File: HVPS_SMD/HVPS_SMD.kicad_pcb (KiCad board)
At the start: 2 copper layers, 30 x 20 mm, 18 parts, among them J1 CONN_01X02, J2 CONN_01X02, Q1 AO4294, T1 MagTop-HVSMPS, U1 LM3478SOIC8

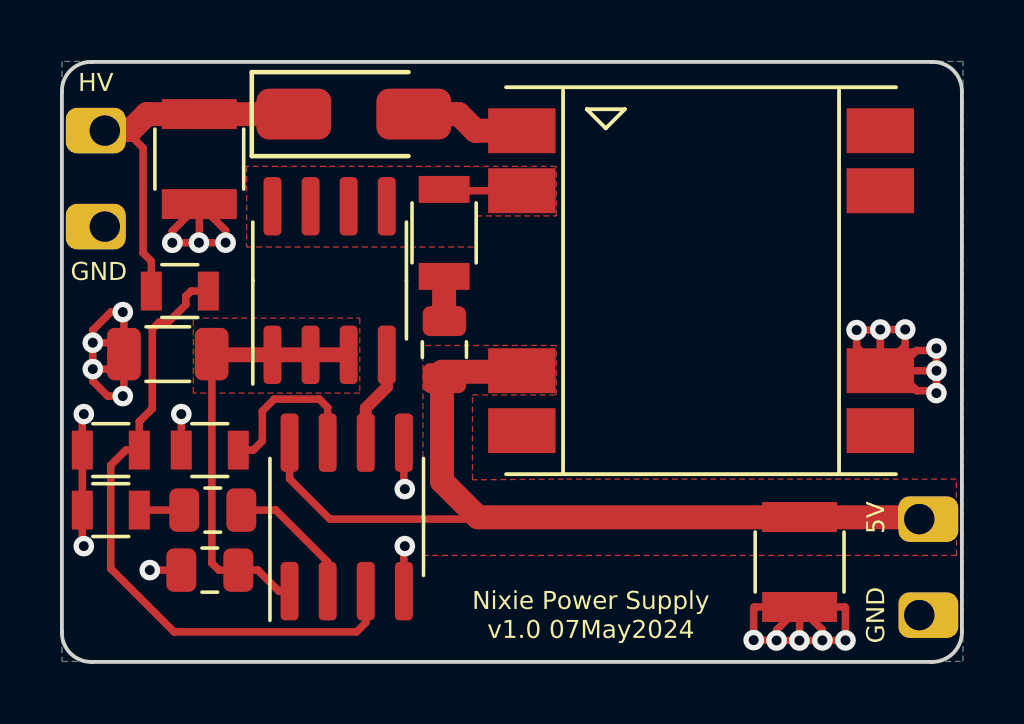
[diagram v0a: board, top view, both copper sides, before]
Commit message: Add fiducials and external control options
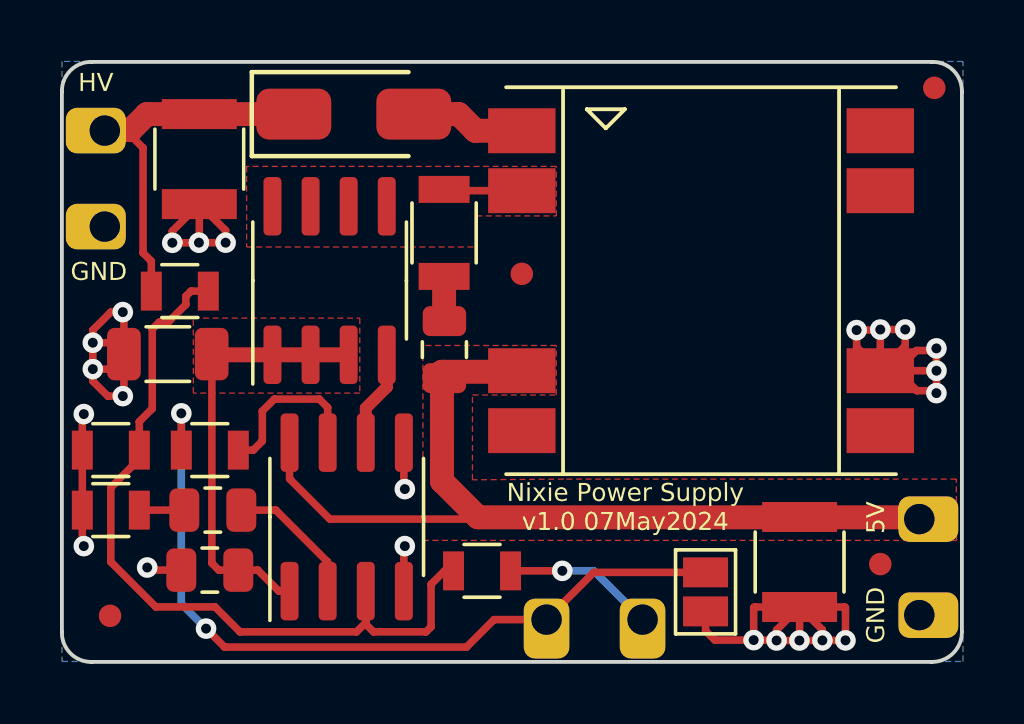
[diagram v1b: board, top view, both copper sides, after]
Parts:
- removed G***: LOGO-Nixieclock.biz, NixieClockMaster:LOGO-Nixieclock.biz
- added FID1: Fiducial, Fiducial:Fiducial_0.75mm_Mask1.5mm, F.Cu at (212.3, 77.9)
- added FID2: Fiducial, Fiducial:Fiducial_0.75mm_Mask1.5mm, F.Cu at (214.2, 62.0)
- added FID3: Fiducial, Fiducial:Fiducial_0.75mm_Mask1.5mm, F.Cu at (200.4, 68.2)
- added FID4: Fiducial, Fiducial:Fiducial_0.75mm_Mask1.5mm, F.Cu at (186.7, 79.6)
- added J3: CONN_01X02, NixieClockMaster:Header_MA02-Edge-3.2, F.Cu at (202.8, 79.8)
- added JP1: Jumper_2_Open, NixieClockMaster:SolderJumper-2_P1.3mm_Open_Pad1.0x1.5mm_NoCtYd, F.Cu at (206.5, 78.8)
- added R2: 15k, lib_fp:R_0805, F.Cu at (199.1, 78.1)
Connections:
- Rf1 pad 1: GND -> SHDN
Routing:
- net SHDN: track 0.00 -> 26.7 mm, vias 0 -> 2
- net Net-(R1-Pad2): track 21.9 -> 27.3 mm
- net Rext: track 0.00 -> 5.07 mm, vias 0 -> 1
- net GND: track 50.4 -> 51.7 mm, vias 24 -> 23

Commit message: Silk screen and QR Code
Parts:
- added G***: LOGO, NixieClockMaster:LOGO-Nixieclock-small.biz, B.Cu at (200.5, 69.1)
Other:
- board text added: "Thanks to nixies.us www.nixieclock.biz"

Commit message: Correct LCSC Part #
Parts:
- moved FID3 103.4 mm to (115.3, 127.1)
- moved FID4 103.4 mm to (101.6, 138.5)
- moved Rs1 103.4 mm to (112.7, 125.7)
- moved C2 103.4 mm to (104.9, 136.9)
- moved C3 103.4 mm to (104.6, 123.2)
- moved Cc1 103.4 mm to (105.0, 134.9)
- moved Cs1 103.4 mm to (112.8, 129.6)
- moved D1 103.4 mm to (109.7, 121.7)
- moved FID1 103.4 mm to (127.3, 136.7)
- moved FID2 103.4 mm to (129.1, 120.9)
- moved G*** 103.4 mm to (115.4, 127.9)
- moved J1 103.4 mm to (128.6, 136.8)
- moved J2 103.4 mm to (101.4, 123.9)
- moved J3 103.4 mm to (117.8, 138.6)
- moved JP1 103.4 mm to (121.5, 137.7)
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
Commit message: Hand Assembly aid
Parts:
- U1: value LM3478SOIC8 -> 3478
